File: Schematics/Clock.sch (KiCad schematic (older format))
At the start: 27 parts

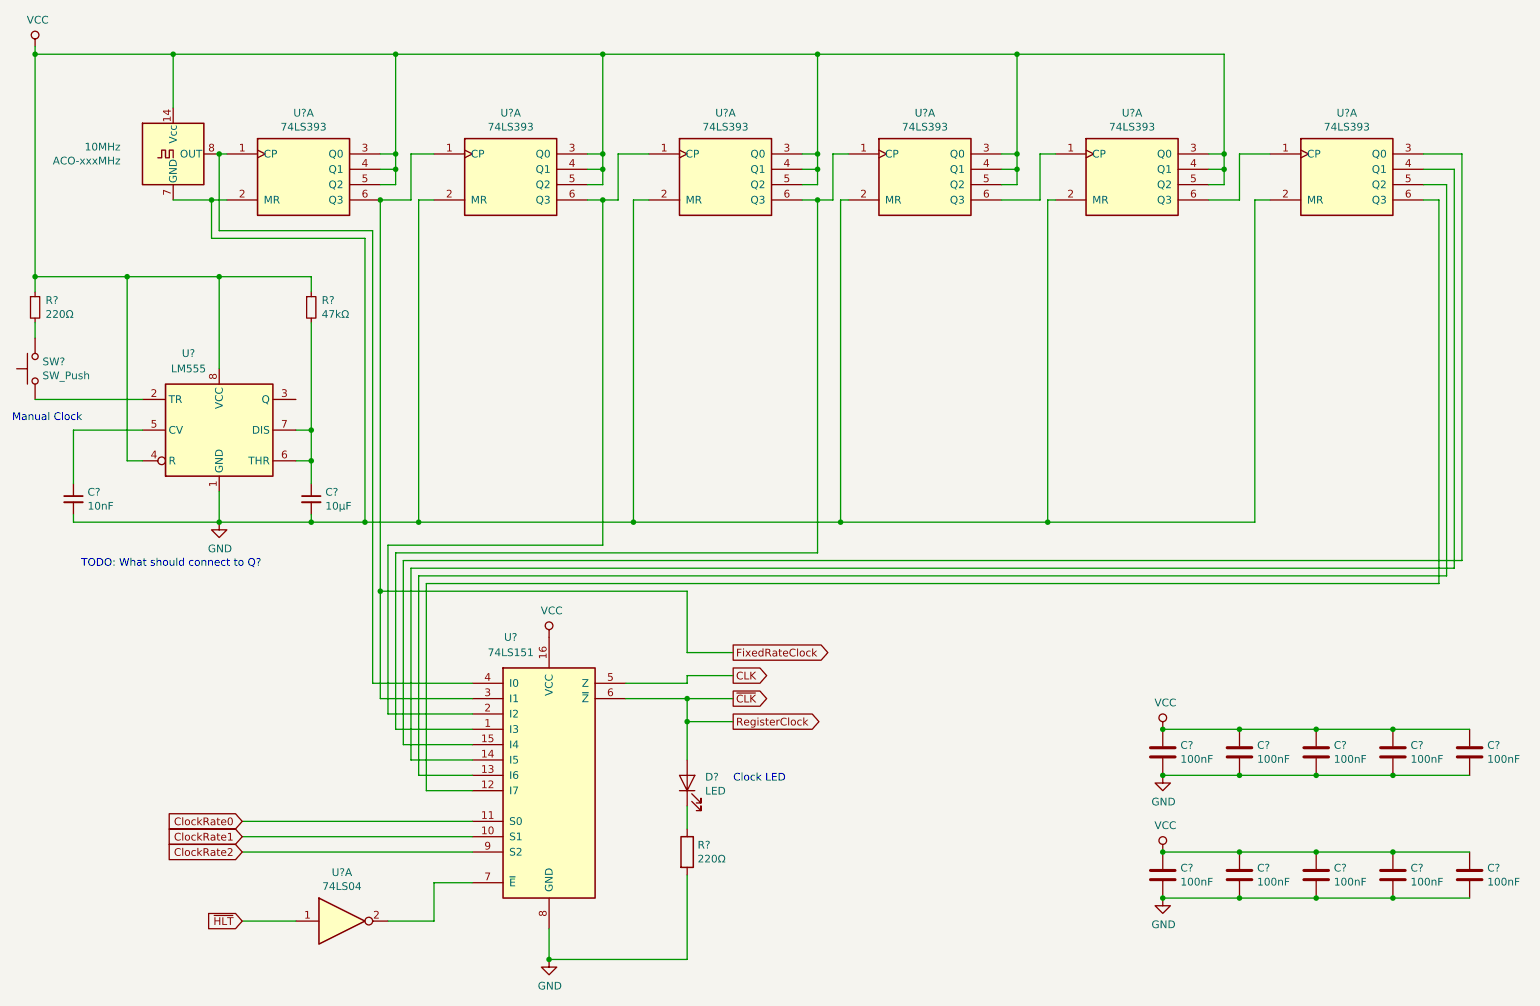
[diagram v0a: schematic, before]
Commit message: Connect the manual clock signal
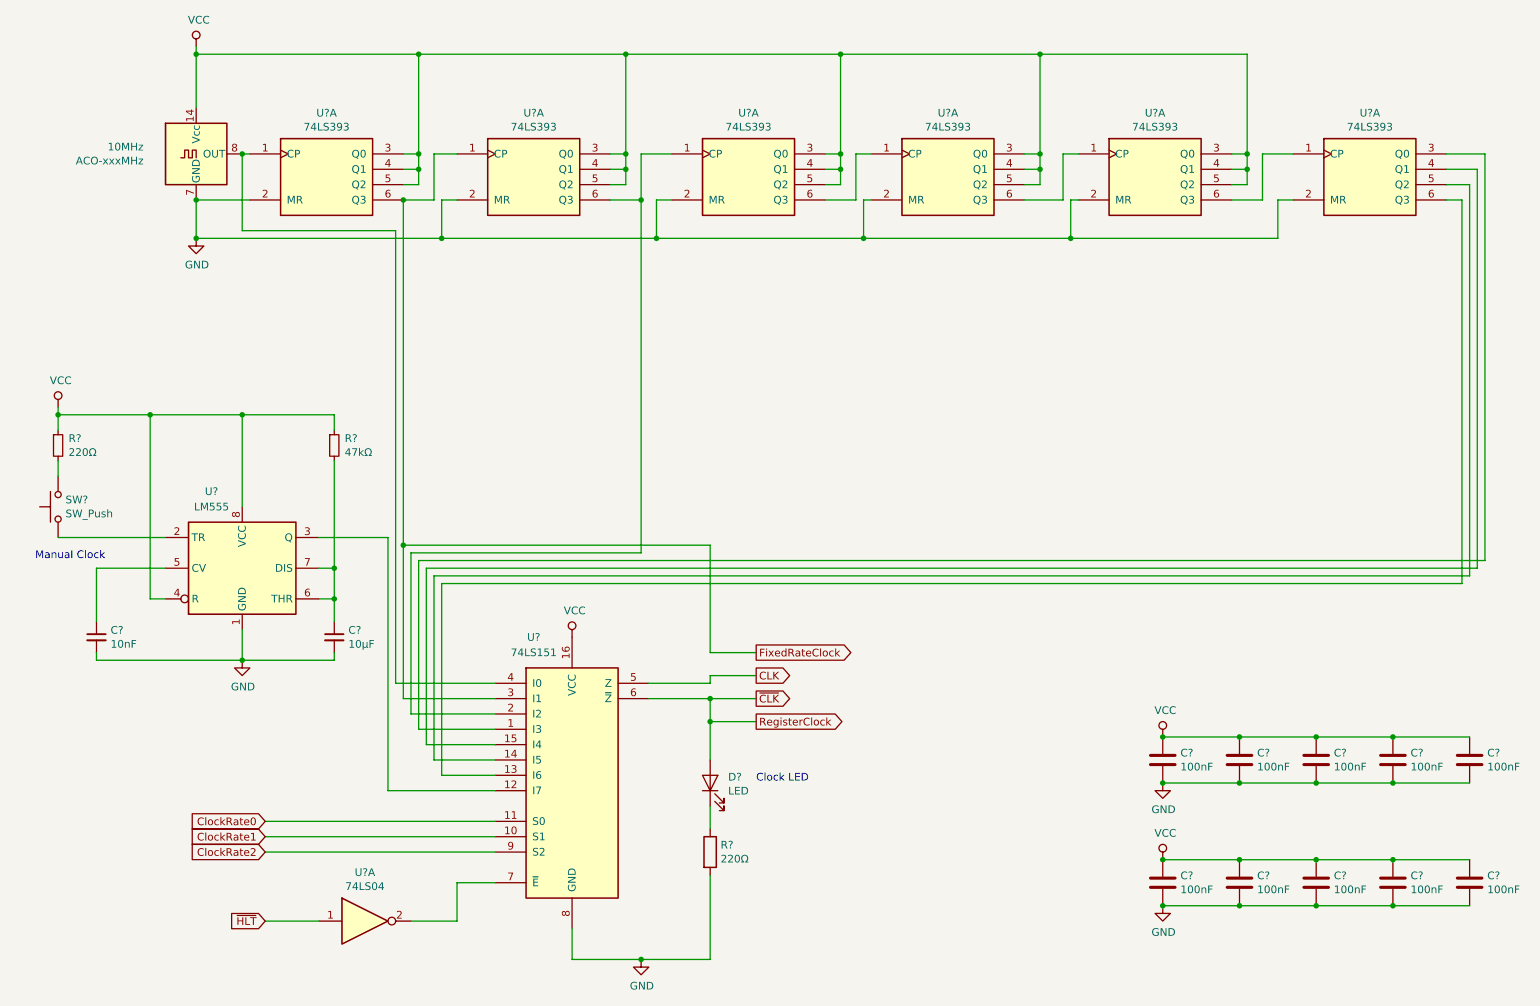
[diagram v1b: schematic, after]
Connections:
- net at U?.1 (CP), U?.6 (Q3): no longer U?.1 (I3)
- net at U?.3 (Q): now also U?.12 (I7)
- net at U?.3 (Q0): now also U?.1 (I3); no longer U?.15 (I4)
- net at U?.4 (Q1): now also U?.15 (I4); no longer U?.14 (I5)
- net at U?.5 (Q2): now also U?.14 (I5); no longer U?.13 (I6)
- net at U?.6 (Q3): now also U?.13 (I6); no longer U?.12 (I7)
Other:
- note removed: "TODO: What should connect to Q?"
- moved on the sheet: 10MHz, C?, D?, R?, SW?, U?, U?A

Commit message: annotate
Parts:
- gave numbers to parts that had none: 26
- renumbered 10MHz to 10MHz1
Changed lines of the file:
@@
 $EndDescr
 $Comp
-L Oscillator:ACO-xxxMHz 10MHz
+L Oscillator:ACO-xxxMHz 10MHz1
 U 1 1 5D387BCA
 P 1700 1450
-F 0 "10MHz" H 1357 1496 50  0000 R CNN
+F 0 "10MHz1" H 1357 1496 50  0000 R CNN
 F 1 "ACO-xxxMHz" H 1357 1405 50  0000 R CNN
 F 2 "Oscillator:Oscillator_DIP-14" H 2150 1100 50  0001 C CNN
@@
 $EndComp
 $Comp
-L 74xx:74LS393 U?
+L 74xx:74LS393 U67
 U 1 1 5D3898BC
 P 2550 1550
-F 0 "U?" H 2550 1917 50  0000 C CNN
+F 0 "U67" H 2550 1917 50  0000 C CNN
 F 1 "74LS393" H 2550 1826 50  0000 C CNN
 F 2 "" H 2550 1550 50  0001 C CNN
@@
 $EndComp
 $Comp
-L 74xx:74LS393 U?
+L 74xx:74LS393 U71
 U 1 1 5D38C231
 P 5300 1550
-F 0 "U?" H 5300 1917 50  0000 C CNN
+F 0 "U71" H 5300 1917 50  0000 C CNN
 F 1 "74LS393" H 5300 1826 50  0000 C CNN
 F 2 "" H 5300 1550 50  0001 C CNN
@@
 $EndComp
 $Comp
-L 74xx:74LS393 U?
+L 74xx:74LS393 U72
 U 1 1 5D38D960
 P 6600 1550
-F 0 "U?" H 6600 1917 50  0000 C CNN
+F 0 "U72" H 6600 1917 50  0000 C CNN
 F 1 "74LS393" H 6600 1826 50  0000 C CNN
 F 2 "" H 6600 1550 50  0001 C CNN
@@
 $EndComp
 $Comp
-L 74xx:74LS393 U?
+L 74xx:74LS393 U73
 U 1 1 5D38E544
 P 7950 1550
-F 0 "U?" H 7950 1917 50  0000 C CNN
+F 0 "U73" H 7950 1917 50  0000 C CNN
 F 1 "74LS393" H 7950 1826 50  0000 C CNN
 F 2 "" H 7950 1550 50  0001 C CNN
@@
 $EndComp
 $Comp
-L Timer:LM555 U?
+L Timer:LM555 U66
 U 1 1 5D38F3A1
 P 2000 4150
-F 0 "U?" H 1800 4650 50  0000 C CNN
+F 0 "U66" H 1800 4650 50  0000 C CNN
 F 1 "LM555" H 1800 4550 50  0000 C CNN
 F 2 "" H 2000 4150 50  0001 C CNN
@@
 $EndComp
 $Comp
-L Device:C_Small C?
+L Device:C_Small C56
 U 1 1 5D393902
 P 1050 4600
-F 0 "C?" H 1142 4646 50  0000 L CNN
+F 0 "C56" H 1142 4646 50  0000 L CNN
 F 1 "10nF" H 1142 4555 50  0000 L CNN
 F 2 "" H 1050 4600 50  0001 C CNN
@@
 $EndComp
 $Comp
-L Device:C_Small C?
+L Device:C_Small C57
 U 1 1 5D394118
 P 2600 4600
-F 0 "C?" H 2692 4646 50  0000 L CNN
+F 0 "C57" H 2692 4646 50  0000 L CNN
 F 1 "10µF" H 2692 4555 50  0000 L CNN
 F 2 "" H 2600 4600 50  0001 C CNN
@@
 	7350 1450 7450 1450
 $Comp
-L 74xx:74LS393 U?
+L 74xx:74LS393 U74
 U 1 1 5D3C15D2
 P 9350 1550
-F 0 "U?" H 9350 1917 50  0000 C CNN
+F 0 "U74" H 9350 1917 50  0000 C CNN
 F 1 "74LS393" H 9350 1826 50  0000 C CNN
 F 2 "" H 9350 1550 50  0001 C CNN
@@
 Connection ~ 7200 800
 $Comp
-L 74xx:74LS393 U?
+L 74xx:74LS393 U69
 U 1 1 5D38B39F
 P 3900 1550
-F 0 "U?" H 3900 1917 50  0000 C CNN
+F 0 "U69" H 3900 1917 50  0000 C CNN
 F 1 "74LS393" H 3900 1826 50  0000 C CNN
 F 2 "" H 3900 1550 50  0001 C CNN
@@
 ~CLK
 $Comp
-L Device:R R?
+L Device:R R88
 U 1 1 5D43460F
 P 5050 6000
-F 0 "R?" H 5118 6046 50  0000 L CNN
+F 0 "R88" H 5118 6046 50  0000 L CNN
 F 1 "220Ω" H 5118 5955 50  0000 L CNN
 F 2 "" V 5090 5990 50  0001 C CNN
@@
 $EndComp
 $Comp
-L Device:LED D?
+L Device:LED D72
 U 1 1 5D42B044
 P 5050 5550
-F 0 "D?" V 5089 5433 50  0000 R CNN
+F 0 "D72" V 5089 5433 50  0000 R CNN
 F 1 "LED" V 4998 5433 50  0000 R CNN
 F 2 "" H 5050 5550 50  0001 C CNN
@@
 	1700 1750 2050 1750
 $Comp
-L 74xx:74LS151 U?
+L 74xx:74LS151 U70
 U 1 1 5D3FEA17
 P 4150 5500
-F 0 "U?" H 3900 6400 50  0000 C CNN
+F 0 "U70" H 3900 6400 50  0000 C CNN
 F 1 "74LS151" H 3900 6300 50  0000 C CNN
 F 2 "" H 4150 5500 50  0001 C CNN
@@
 	5050 4850 5350 4850
 $Comp
-L power:VCC #PWR?
+L power:VCC #PWR0249
 U 1 1 5D90C7E6
 P 4150 4600
-F 0 "#PWR?" H 4150 4450 50  0001 C CNN
+F 0 "#PWR0249" H 4150 4450 50  0001 C CNN
 F 1 "VCC" H 4167 4773 50  0000 C CNN
 F 2 "" H 4150 4600 50  0001 C CNN
@@
 $EndComp
 $Comp
-L power:GND #PWR?
+L power:GND #PWR0250
 U 1 1 5D919C2F
 P 2000 4750
-F 0 "#PWR?" H 2000 4500 50  0001 C CNN
+F 0 "#PWR0250" H 2000 4500 50  0001 C CNN
 F 1 "GND" H 2005 4577 50  0000 C CNN
 F 2 "" H 2000 4750 50  0001 C CNN
@@
 $EndComp
 $Comp
-L power:GND #PWR?
+L power:GND #PWR0251
 U 1 1 5D91A0CA
 P 4600 6700
-F 0 "#PWR?" H 4600 6450 50  0001 C CNN
+F 0 "#PWR0251" H 4600 6450 50  0001 C CNN
 F 1 "GND" H 4605 6527 50  0000 C CNN
 F 2 "" H 4600 6700 50  0001 C CNN
@@
 	3050 4000 3050 5000
 $Comp
-L Device:C C?
+L Device:C C58
 U 1 1 5D934C27
 P 8000 5400
-F 0 "C?" H 8115 5446 50  0000 L CNN
+F 0 "C58" H 8115 5446 50  0000 L CNN
 F 1 "100nF" H 8115 5355 50  0000 L CNN
 F 2 "" H 8038 5250 50  0001 C CNN
@@
 $EndComp
 $Comp
-L Device:C C?
+L Device:C C60
 U 1 1 5D935B94
 P 8500 5400
-F 0 "C?" H 8615 5446 50  0000 L CNN
+F 0 "C60" H 8615 5446 50  0000 L CNN
 F 1 "100nF" H 8615 5355 50  0000 L CNN
 F 2 "" H 8538 5250 50  0001 C CNN
@@
 $EndComp
 $Comp
-L Device:C C?
+L Device:C C62
 U 1 1 5D935F32
 P 9000 5400
-F 0 "C?" H 9115 5446 50  0000 L CNN
+F 0 "C62" H 9115 5446 50  0000 L CNN
 F 1 "100nF" H 9115 5355 50  0000 L CNN
 F 2 "" H 9038 5250 50  0001 C CNN
@@
 $EndComp
 $Comp
-L Device:C C?
+L Device:C C64
 U 1 1 5D936485
 P 9500 5400
-F 0 "C?" H 9615 5446 50  0000 L CNN
+F 0 "C64" H 9615 5446 50  0000 L CNN
 F 1 "100nF" H 9615 5355 50  0000 L CNN
 F 2 "" H 9538 5250 50  0001 C CNN
@@
 $EndComp
 $Comp
-L Device:C C?
+L Device:C C66
 U 1 1 5D93673D
 P 10000 5400
-F 0 "C?" H 10115 5446 50  0000 L CNN
+F 0 "C66" H 10115 5446 50  0000 L CNN
 F 1 "100nF" H 10115 5355 50  0000 L CNN
 F 2 "" H 10038 5250 50  0001 C CNN
@@
 $EndComp
 $Comp
-L power:GND #PWR?
+L power:GND #PWR0252
 U 1 1 5D936CDD
 P 8000 5550
-F 0 "#PWR?" H 8000 5300 50  0001 C CNN
+F 0 "#PWR0252" H 8000 5300 50  0001 C CNN
 F 1 "GND" H 8005 5377 50  0000 C CNN
 F 2 "" H 8000 5550 50  0001 C CNN
@@
 $EndComp
 $Comp
-L power:VCC #PWR?
+L power:VCC #PWR0253
 U 1 1 5D937A39
 P 8000 5250
-F 0 "#PWR?" H 8000 5100 50  0001 C CNN
+F 0 "#PWR0253" H 8000 5100 50  0001 C CNN
 F 1 "VCC" H 8017 5423 50  0000 C CNN
 F 2 "" H 8000 5250 50  0001 C CNN
@@
 Connection ~ 8000 5550
 $Comp
-L Device:C C?
+L Device:C C59
 U 1 1 5D9721DB
 P 8000 6200
-F 0 "C?" H 8115 6246 50  0000 L CNN
+F 0 "C59" H 8115 6246 50  0000 L CNN
 F 1 "100nF" H 8115 6155 50  0000 L CNN
 F 2 "" H 8038 6050 50  0001 C CNN
@@
 $EndComp
 $Comp
-L Device:C C?
+L Device:C C61
 U 1 1 5D9721E1
 P 8500 6200
-F 0 "C?" H 8615 6246 50  0000 L CNN
+F 0 "C61" H 8615 6246 50  0000 L CNN
 F 1 "100nF" H 8615 6155 50  0000 L CNN
 F 2 "" H 8538 6050 50  0001 C CNN
@@
 $EndComp
 $Comp
-L Device:C C?
+L Device:C C63
 U 1 1 5D9721E7
 P 9000 6200
-F 0 "C?" H 9115 6246 50  0000 L CNN
+F 0 "C63" H 9115 6246 50  0000 L CNN
 F 1 "100nF" H 9115 6155 50  0000 L CNN
 F 2 "" H 9038 6050 50  0001 C CNN
@@
 $EndComp
 $Comp
-L Device:C C?
+L Device:C C65
 U 1 1 5D9721ED
 P 9500 6200
-F 0 "C?" H 9615 6246 50  0000 L CNN
+F 0 "C65" H 9615 6246 50  0000 L CNN
 F 1 "100nF" H 9615 6155 50  0000 L CNN
 F 2 "" H 9538 6050 50  0001 C CNN
@@
 $EndComp
 $Comp
-L Device:C C?
+L Device:C C67
 U 1 1 5D9721F3
 P 10000 6200
-F 0 "C?" H 10115 6246 50  0000 L CNN
+F 0 "C67" H 10115 6246 50  0000 L CNN
 F 1 "100nF" H 10115 6155 50  0000 L CNN
 F 2 "" H 10038 6050 50  0001 C CNN
@@
 $EndComp
 $Comp
-L power:GND #PWR?
+L power:GND #PWR0254
 U 1 1 5D9721F9
 P 8000 6350
-F 0 "#PWR?" H 8000 6100 50  0001 C CNN
+F 0 "#PWR0254" H 8000 6100 50  0001 C CNN
 F 1 "GND" H 8005 6177 50  0000 C CNN
 F 2 "" H 8000 6350 50  0001 C CNN
@@
 $EndComp
 $Comp
-L power:VCC #PWR?
+L power:VCC #PWR0255
 U 1 1 5D9721FF
 P 8000 6050
-F 0 "#PWR?" H 8000 5900 50  0001 C CNN
+F 0 "#PWR0255" H 8000 5900 50  0001 C CNN
 F 1 "VCC" H 8017 6223 50  0000 C CNN
 F 2 "" H 8000 6050 50  0001 C CNN
@@
 	2600 3450 2600 4150
 $Comp
-L Device:R_Small R?
+L Device:R_Small R87
 U 1 1 5D39244B
 P 2600 3350
-F 0 "R?" H 2668 3396 50  0000 L CNN
+F 0 "R87" H 2668 3396 50  0000 L CNN
 F 1 "47kΩ" H 2668 3305 50  0000 L CNN
 F 2 "" H 2600 3350 50  0001 C CNN
@@
 $EndComp
 $Comp
-L Device:R_Small R?
+L Device:R_Small R86
 U 1 1 5D39306C
 P 800 3350
-F 0 "R?" H 868 3396 50  0000 L CNN
+F 0 "R86" H 868 3396 50  0000 L CNN
 F 1 "220Ω" H 868 3305 50  0000 L CNN
 F 2 "" H 800 3350 50  0001 C CNN
@@
 $EndComp
 $Comp
-L Switch:SW_Push SW?
+L Switch:SW_Push SW1
 U 1 1 5D843F11
 P 800 3750
-F 0 "SW?" V 846 3702 50  0000 R CNN
+F 0 "SW1" V 846 3702 50  0000 R CNN
 F 1 "SW_Push" V 755 3702 50  0000 R CNN
 F 2 "" H 800 3950 50  0001 C CNN
@@
 	3300 1750 3300 2000
 $Comp
-L power:GND #PWR?
+L power:GND #PWR0256
 U 1 1 5D888695
 P 1700 2000
-F 0 "#PWR?" H 1700 1750 50  0001 C CNN
+F 0 "#PWR0256" H 1700 1750 50  0001 C CNN
 F 1 "GND" H 1705 1827 50  0000 C CNN
 F 2 "" H 1700 2000 50  0001 C CNN
@@
 	1700 2000 3300 2000
 $Comp
-L power:VCC #PWR?
+L power:VCC #PWR0257
 U 1 1 5D3986DC
 P 1700 750
-F 0 "#PWR?" H 1700 600 50  0001 C CNN
+F 0 "#PWR0257" H 1700 600 50  0001 C CNN
 F 1 "VCC" H 1717 923 50  0000 C CNN
 F 2 "" H 1700 750 50  0001 C CNN
@@
 	1700 750  1700 800
 $Comp
-L power:VCC #PWR?
+L power:VCC #PWR0258
 U 1 1 5D8FB444
 P 800 3100
-F 0 "#PWR?" H 800 2950 50  0001 C CNN
+F 0 "#PWR0258" H 800 2950 50  0001 C CNN
 F 1 "VCC" H 817 3273 50  0000 C CNN
 F 2 "" H 800 3100 50  0001 C CNN
@@
 	3100 6450 3400 6450
 $Comp
-L 74xx:74LS04 U?
+L 74xx:74LS04 U68
 U 1 1 5D7C9FC5
 P 2800 6450
-F 0 "U?" H 2800 6767 50  0000 C CNN
+F 0 "U68" H 2800 6767 50  0000 C CNN
 F 1 "74LS04" H 2800 6676 50  0000 C CNN
 F 2 "" H 2800 6450 50  0001 C CNN

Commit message: Add footprints to all decoupling caps
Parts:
- C56, C58, C59, C60, C61, C62, C63, C64, C65, C66, C67: footprint (none) -> Capacitor_THT:C_Disc_D4.3mm_W1.9mm_P5.00mm
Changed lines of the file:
@@
 F 0 "C56" H 1142 4646 50  0000 L CNN
 F 1 "10nF" H 1142 4555 50  0000 L CNN
-F 2 "" H 1050 4600 50  0001 C CNN
+F 2 "Capacitor_THT:C_Disc_D4.3mm_W1.9mm_P5.00mm" H 1050 4600 50  0001 C CNN
 F 3 "~" H 1050 4600 50  0001 C CNN
 	1    1050 4600
@@
 F 0 "C58" H 8115 5446 50  0000 L CNN
 F 1 "100nF" H 8115 5355 50  0000 L CNN
-F 2 "" H 8038 5250 50  0001 C CNN
+F 2 "Capacitor_THT:C_Disc_D4.3mm_W1.9mm_P5.00mm" H 8038 5250 50  0001 C CNN
 F 3 "~" H 8000 5400 50  0001 C CNN
 	1    8000 5400
@@
 F 0 "C60" H 8615 5446 50  0000 L CNN
 F 1 "100nF" H 8615 5355 50  0000 L CNN
-F 2 "" H 8538 5250 50  0001 C CNN
+F 2 "Capacitor_THT:C_Disc_D4.3mm_W1.9mm_P5.00mm" H 8538 5250 50  0001 C CNN
 F 3 "~" H 8500 5400 50  0001 C CNN
 	1    8500 5400
@@
 F 0 "C62" H 9115 5446 50  0000 L CNN
 F 1 "100nF" H 9115 5355 50  0000 L CNN
-F 2 "" H 9038 5250 50  0001 C CNN
+F 2 "Capacitor_THT:C_Disc_D4.3mm_W1.9mm_P5.00mm" H 9038 5250 50  0001 C CNN
 F 3 "~" H 9000 5400 50  0001 C CNN
 	1    9000 5400
@@
 F 0 "C64" H 9615 5446 50  0000 L CNN
 F 1 "100nF" H 9615 5355 50  0000 L CNN
-F 2 "" H 9538 5250 50  0001 C CNN
+F 2 "Capacitor_THT:C_Disc_D4.3mm_W1.9mm_P5.00mm" H 9538 5250 50  0001 C CNN
 F 3 "~" H 9500 5400 50  0001 C CNN
 	1    9500 5400
@@
 F 0 "C66" H 10115 5446 50  0000 L CNN
 F 1 "100nF" H 10115 5355 50  0000 L CNN
-F 2 "" H 10038 5250 50  0001 C CNN
+F 2 "Capacitor_THT:C_Disc_D4.3mm_W1.9mm_P5.00mm" H 10038 5250 50  0001 C CNN
 F 3 "~" H 10000 5400 50  0001 C CNN
 	1    10000 5400
@@
 F 0 "C59" H 8115 6246 50  0000 L CNN
 F 1 "100nF" H 8115 6155 50  0000 L CNN
-F 2 "" H 8038 6050 50  0001 C CNN
+F 2 "Capacitor_THT:C_Disc_D4.3mm_W1.9mm_P5.00mm" H 8038 6050 50  0001 C CNN
 F 3 "~" H 8000 6200 50  0001 C CNN
 	1    8000 6200
@@
 F 0 "C61" H 8615 6246 50  0000 L CNN
 F 1 "100nF" H 8615 6155 50  0000 L CNN
-F 2 "" H 8538 6050 50  0001 C CNN
+F 2 "Capacitor_THT:C_Disc_D4.3mm_W1.9mm_P5.00mm" H 8538 6050 50  0001 C CNN
 F 3 "~" H 8500 6200 50  0001 C CNN
 	1    8500 6200
@@
 F 0 "C63" H 9115 6246 50  0000 L CNN
 F 1 "100nF" H 9115 6155 50  0000 L CNN
-F 2 "" H 9038 6050 50  0001 C CNN
+F 2 "Capacitor_THT:C_Disc_D4.3mm_W1.9mm_P5.00mm" H 9038 6050 50  0001 C CNN
 F 3 "~" H 9000 6200 50  0001 C CNN
 	1    9000 6200
@@
 F 0 "C65" H 9615 6246 50  0000 L CNN
 F 1 "100nF" H 9615 6155 50  0000 L CNN
-F 2 "" H 9538 6050 50  0001 C CNN
+F 2 "Capacitor_THT:C_Disc_D4.3mm_W1.9mm_P5.00mm" H 9538 6050 50  0001 C CNN
 F 3 "~" H 9500 6200 50  0001 C CNN
 	1    9500 6200
@@
 F 0 "C67" H 10115 6246 50  0000 L CNN
 F 1 "100nF" H 10115 6155 50  0000 L CNN
-F 2 "" H 10038 6050 50  0001 C CNN
+F 2 "Capacitor_THT:C_Disc_D4.3mm_W1.9mm_P5.00mm" H 10038 6050 50  0001 C CNN
 F 3 "~" H 10000 6200 50  0001 C CNN
 	1    10000 6200

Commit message: Add footprint for radial capacitor in clock circuit.
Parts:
- C57: footprint (none) -> Capacitor_THT:CP_Radial_D5.0mm_P2.00mm; symbol Device:C_Small -> Device:CP1
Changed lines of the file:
@@
-$EndComp
-$Comp
-L Timer:LM555 U66
-U 1 1 5D38F3A1
-P 2000 4150
-F 0 "U66" H 1800 4650 50  0000 C CNN
-F 1 "LM555" H 1800 4550 50  0000 C CNN
-F 2 "" H 2000 4150 50  0001 C CNN
-F 3 "http://www.ti.com/lit/ds/symlink/lm555.pdf" H 2000 4150 50  0001 C CNN
-	1    2000 4150
-	1    0    0    -1
 $EndComp
 $Comp
@@
 $EndComp
 $Comp
-L Device:C_Small C57
+L Device:CP1 C57
 U 1 1 5D394118
-P 2600 4600
-F 0 "C57" H 2692 4646 50  0000 L CNN
-F 1 "10µF" H 2692 4555 50  0000 L CNN
-F 2 "" H 2600 4600 50  0001 C CNN
-F 3 "~" H 2600 4600 50  0001 C CNN
-	1    2600 4600
+P 2600 4550
+F 0 "C57" H 2692 4596 50  0000 L CNN
+F 1 "10µF" H 2692 4505 50  0000 L CNN
+F 2 "Capacitor_THT:CP_Radial_D5.0mm_P2.00mm" H 2600 4550 50  0001 C CNN
+F 3 "~" H 2600 4550 50  0001 C CNN
+	1    2600 4550
 	1    0    0    -1
 $EndComp
@@
 	2000 3150 2600 3150
 Connection ~ 2000 3150
-Wire Wire Line
-	2600 4350 2600 4500
-Connection ~ 2600 4350
 Wire Wire Line
 	1700 1150 1700 800
@@
 Wire Wire Line
 	4600 6700 5050 6700
+$Comp
+L Timer:LM555 U66
+U 1 1 5D38F3A1
+P 2000 4150
+F 0 "U66" H 1800 4650 50  0000 C CNN
+F 1 "LM555" H 1800 4550 50  0000 C CNN
+F 2 "" H 2000 4150 50  0001 C CNN
+F 3 "http://www.ti.com/lit/ds/symlink/lm555.pdf" H 2000 4150 50  0001 C CNN
+	1    2000 4150
+	1    0    0    -1
+$EndComp
+Wire Wire Line
+	2600 4350 2600 4400
+Connection ~ 2600 4350
 $EndSCHEMATC
